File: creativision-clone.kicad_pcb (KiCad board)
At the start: 2 copper layers, 205.7 x 99.7 mm, 103 parts, among them J1 Conn_01x10_Socket, J2 Conn_01x10_Socket, J3 Conn_01x07_Pin, J4 Conn_01x04_Socket, J5 RCJ-013, J6 RCJ-014, P1 Cartridge Slot, Q1 2n4401, SW1 Reset, SW2 Power Toggle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

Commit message: Data bus and control signals laid out on cart
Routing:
- net -5V: track 0.00 -> 136.7 mm, vias 0 -> 2
- net /~{WRAM_CE}: track 35.1 -> 164.5 mm, vias 1 -> 6
- net /~{ROM1}: track 0.00 -> 118.3 mm, vias 0 -> 5
- net /~{ROM_RD}: track 13.4 -> 130.0 mm, vias 2 -> 7
- net /~{ROM0}: track 0.00 -> 105.6 mm, vias 0 -> 2
- net /~{ROM2}: track 0.00 -> 105.2 mm, vias 0 -> 4
- net /R/~{W}: track 136.2 -> 232.8 mm, vias 7 -> 9
- net /AUDIO_IN: track 139.3 -> 233.7 mm, vias 1 -> 3
- net +12V: track 0.00 -> 73.2 mm, vias 0 -> 1
- net /d6: track 176.5 -> 248.5 mm, vias 10 -> 12
- net /Φ2: track 122.6 -> 193.9 mm, vias 4 -> 6
- net /d7: track 198.3 -> 269.0 mm, vias 10 -> 12
- net /d4: track 147.1 -> 207.7 mm, vias 10 -> 12
- net /d5: track 156.6 -> 215.7 mm, vias 8 -> 10
- net /d3: track 153.3 -> 205.7 mm, vias 6 -> 8
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
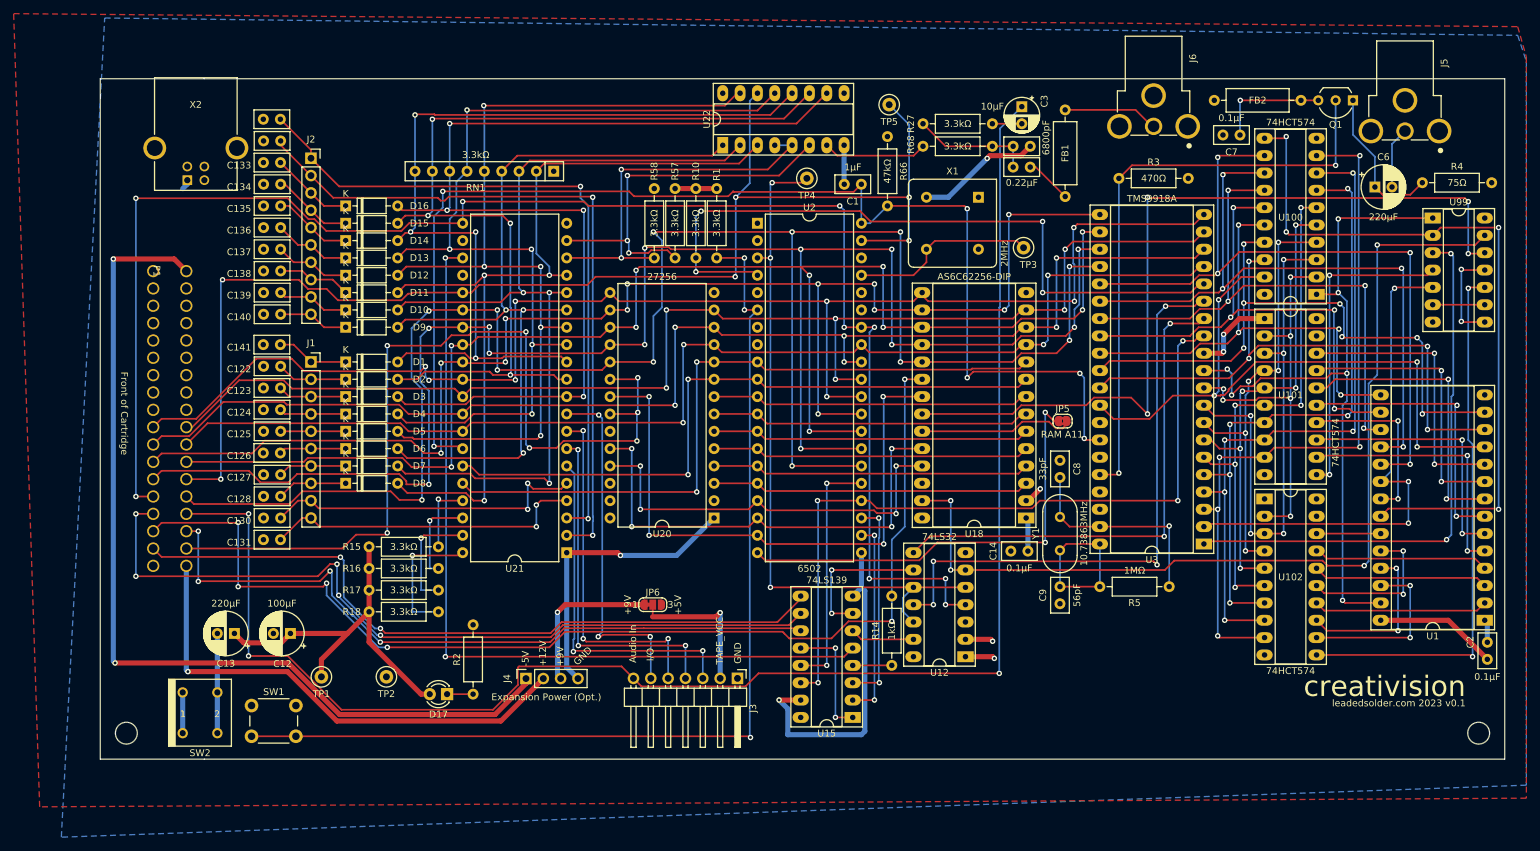
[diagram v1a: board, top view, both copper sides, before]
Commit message: Power pour problems
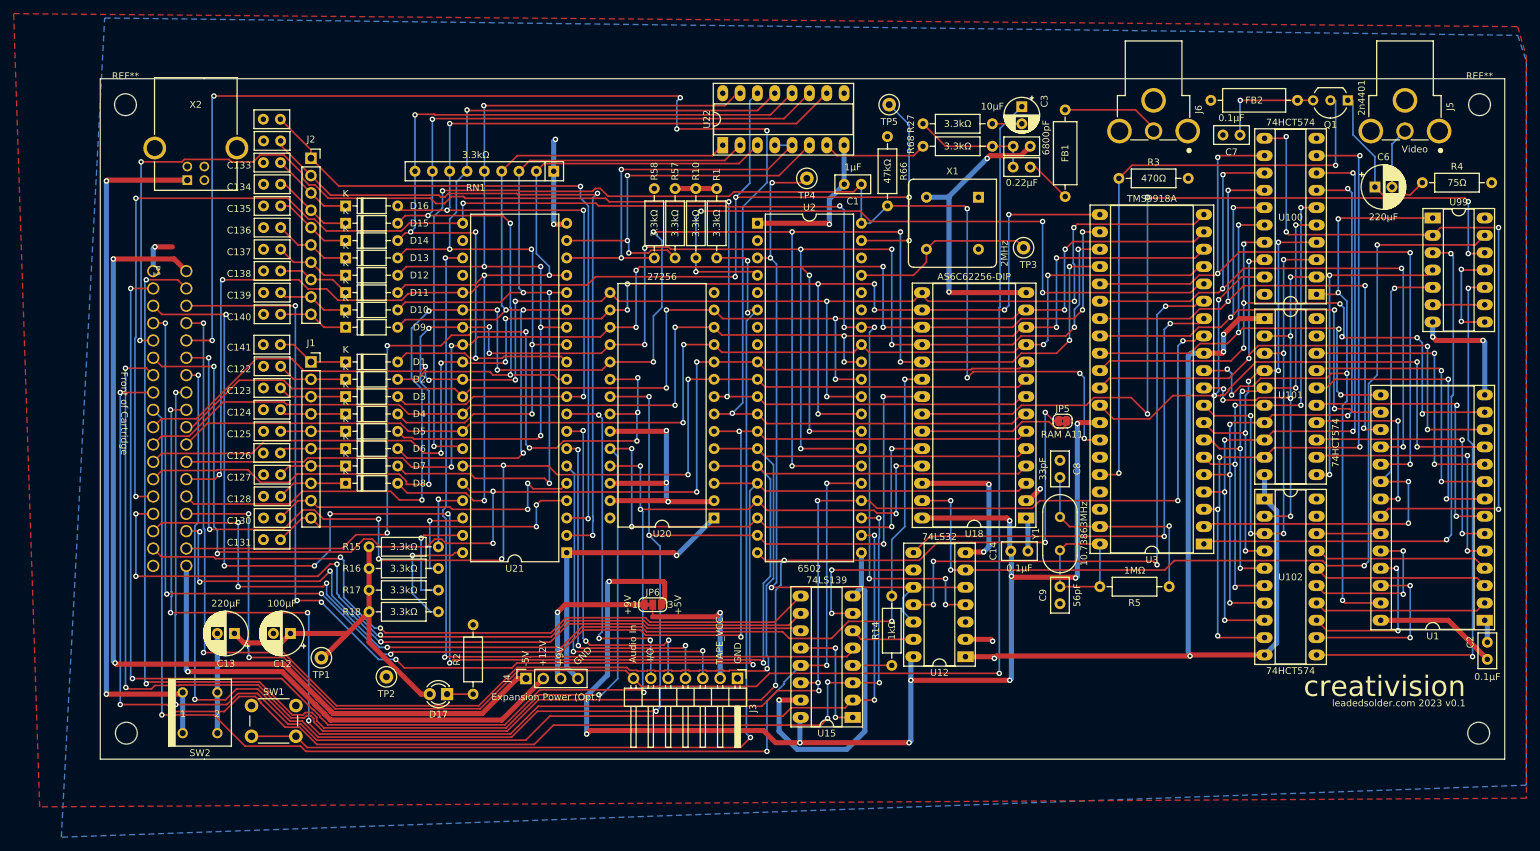
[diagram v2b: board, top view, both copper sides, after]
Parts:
- added REF**: MountingHole_3.2mm_M3, MountingHole:MountingHole_3.2mm_M3, F.Cu at (267.7, 47.4)
- added REF**: MountingHole_3.2mm_M3, MountingHole:MountingHole_3.2mm_M3, F.Cu at (69.3, 47.4)
- moved TP1 2.79 mm to (98.0, 128.4)
- moved Q1 0.76 mm to (248.4, 46.8)
- moved J6 0.69 mm to (220.0, 45.3)
- moved FB2 0.51 mm to (228.3, 46.8)
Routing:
- net GND: track 147.7 -> 389.8 mm, vias 8 -> 18
- net +5V: track 80.5 -> 285.4 mm, vias 0 -> 13
- net /a6: track 46.7 -> 232.2 mm, vias 0 -> 7
- net /a9: track 69.8 -> 245.2 mm, vias 4 -> 7
- net /a5: track 46.7 -> 220.3 mm, vias 0 -> 3
- net /a11: track 65.2 -> 237.0 mm, vias 2 -> 6
- net /a3: track 46.9 -> 216.7 mm, vias 0 -> 6
- net /a13: track 30.7 -> 199.8 mm, vias 2 -> 6
- net /a8: track 60.4 -> 228.0 mm, vias 4 -> 7
- net /a4: track 46.7 -> 208.2 mm, vias 0 -> 6
- net /a7: track 46.7 -> 204.4 mm, vias 0 -> 5
- net /a12: track 29.2 -> 181.7 mm, vias 2 -> 4
- net /a15: track 35.6 -> 186.3 mm, vias 2 -> 4
- net /a10: track 88.3 -> 237.2 mm, vias 4 -> 7
- net /a14: track 110.1 -> 257.9 mm, vias 4 -> 9
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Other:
- board text added: "Video"

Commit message: More plane problems
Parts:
- moved REF** 1.80 mm to (67.6, 47.1)
- moved REF** 1.65 mm to (67.8, 139.5)
- moved REF** 1.52 mm to (269.2, 47.4)
- moved REF** 1.40 mm to (269.0, 139.5)
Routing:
- net GND: track 389.8 -> 415.8 mm
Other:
- board size 205.7 x 99.7 mm -> 208.8 x 99.7 mm
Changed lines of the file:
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@@
         (effects (font (size 1 1) (thickness 0.15)))
     )
-    (fp_text value "AS6C62256-DIP" (at 7.62 35.35) (layer "F.Fab")
+    (fp_text value "AS6C62256-DIP" (at 7.62 35.35) (layer "F.SilkS")
         (effects (font (size 1 1) (thickness 0.15)))
     )
@@
   )
   (footprint "MountingHole:MountingHole_3.2mm_M3" locked (layer "F.Cu")
-    (at 267.59 139.472929)
+    (at 268.987 139.472929)
     (descr "Mounting Hole 3.2mm, no annular, M3")
     (tags "mounting hole 3.2mm no annular m3")
@@
   )
   (footprint "MountingHole:MountingHole_3.2mm_M3" (layer "F.Cu")
-    (at 267.717 47.397929)
+    (at 269.241 47.397929)
     (descr "Mounting Hole 3.2mm, no annular, M3")
     (tags "mounting hole 3.2mm no annular m3")
@@
   )
   (footprint "MountingHole:MountingHole_3.2mm_M3" locked (layer "F.Cu")
-    (at 69.47 139.472929)
+    (at 67.819 139.472929)
     (descr "Mounting Hole 3.2mm, no annular, M3")
     (tags "mounting hole 3.2mm no annular m3")
@@
   )
   (footprint "MountingHole:MountingHole_3.2mm_M3" (layer "F.Cu")
-    (at 69.343 47.397929)
+    (at 67.565 47.143929)
     (descr "Mounting Hole 3.2mm, no annular, M3")
     (tags "mounting hole 3.2mm no annular m3")
@@
     )
   )
-  (gr_line (start 271.4 143.282929) (end 271.4 43.587929)
+  (gr_line (start 65.66 143.282929) (end 64.009 143.282929)
+    (stroke (width 0.1) (type default)) (layer "Edge.Cuts"))
+  (gr_line (start 272.797 143.282929) (end 272.797 43.587929)
+    (stroke (width 0.1) (type default)) (layer "Edge.Cuts"))
+  (gr_line (start 64.009 43.587929) (end 64.009 143.282929)
+    (stroke (width 0.1) (type default)) (layer "Edge.Cuts"))
+  (gr_line (start 272.797 43.587929) (end 271.4 43.587929)
+    (stroke (width 0.1) (type default)) (layer "Edge.Cuts"))
+  (gr_line (start 65.66 43.587929) (end 64.009 43.587929)
     (stroke (width 0.1) (type default)) (layer "Edge.Cuts"))
-  (gr_line (start 65.66 43.587929) (end 65.66 143.282929)
+  (gr_line (start 272.797 143.282929) (end 271.4 143.282929)
     (stroke (width 0.1) (type default)) (layer "Edge.Cuts"))
   (gr_line (start 80.9 43.587929) (end 65.66 43.587929)
@@
   (segment (start 195.835 112.167929) (end 195.073 112.929929) (width 0.75) (layer "B.Cu") (net 2))
   (segment (start 174.625 59.035) (end 174.645 59.055) (width 0.75) (layer "B.Cu") (net 2))
+  (segment (start 225.045 84.227929) (end 225.045 58.192929) (width 0.75) (layer "B.Cu") (net 2))
   (segment (start 195.835 103.023929) (end 195.835 112.167929) (width 0.75) (layer "B.Cu") (net 2))
   (segment (start 172.467 64.923929) (end 172.467 61.233) (width 0.75) (layer "B.Cu") (net 2))
@@
   (segment (start 125.731 139.599929) (end 97.791706 139.599929) (width 0.25) (layer "F.Cu") (net 110))
   (segment (start 177.165 105.41) (end 170.7255 105.41) (width 0.25) (layer "F.Cu") (net 110))
-  (segment (start 226.685 81.275) (end 225.9605 81.9995) (width 0.25) (layer "F.Cu") (net 110))
   (segment (start 96.192905 137.896024) (end 96.192905 137.642023) (width 0.25) (layer "F.Cu") (net 110))
   (segment (start 178.29637 105.41) (end 177.165 105.41) (width 0.25) (layer "F.Cu") (net 110))
   (segment (start 129.795 135.535929) (end 125.731 139.599929) (width 0.25) (layer "F.Cu") (net 110))
   (segment (start 96.013 121.819929) (end 75.947 121.819929) (width 0.25) (layer "F.Cu") (net 110))
-  (segment (start 225.9605 81.9995) (end 224.26226 81.9995) (width 0.25) (layer "F.Cu") (net 110))
+  (segment (start 226.685 81.275) (end 225.9605 81.9995) (width 0.25) (layer "F.Cu") (net 110))
+  (segment (start 225.9605 81.9995) (end 224.0705 81.9995) (width 0.25) (layer "F.Cu") (net 110))
   (segment (start 223.52 105.41) (end 203.28599 105.41) (width 0.25) (layer "F.Cu") (net 110))
   (segment (start 164.847 133.249929) (end 162.561 135.535929) (width 0.25) (layer "F.Cu") (net 110))
@@
   (segment (start 203.28599 105.41) (end 202.16099 106.535) (width 0.25) (layer "F.Cu") (net 110))
   (segment (start 162.561 135.535929) (end 129.795 135.535929) (width 0.25) (layer "F.Cu") (net 110))
-  (segment (start 227.335 81.275) (end 226.685 81.275) (width 0.25) (layer "F.Cu") (net 110))
   (segment (start 202.16099 106.535) (end 179.42137 106.535) (width 0.25) (layer "F.Cu") (net 110))
   (segment (start 97.791706 139.599929) (end 96.140353 137.948576) (width 0.25) (layer "F.Cu") (net 110))
   (segment (start 170.943 133.249929) (end 164.847 133.249929) (width 0.25) (layer "F.Cu") (net 110))
+  (segment (start 227.335 81.275) (end 226.685 81.275) (width 0.25) (layer "F.Cu") (net 110))
   (segment (start 96.140353 137.948576) (end 96.192905 137.896024) (width 0.25) (layer "F.Cu") (net 110))
   (via (at 170.7255 105.41) (size 0.8) (drill 0.4) (layers "F.Cu" "B.Cu") (net 110))
   (via (at 96.192905 137.642023) (size 0.8) (drill 0.4) (layers "F.Cu" "B.Cu") (net 110))
   (via (at 223.52 105.41) (size 0.8) (drill 0.4) (layers "F.Cu" "B.Cu") (net 110))
-  (via (at 224.26226 81.9995) (size 0.8) (drill 0.4) (layers "F.Cu" "B.Cu") (net 110))
+  (via (at 224.0705 81.9995) (size 0.8) (drill 0.4) (layers "F.Cu" "B.Cu") (net 110))
   (via (at 96.013 121.819929) (size 0.8) (drill 0.4) (layers "F.Cu" "B.Cu") (net 110))
   (via (at 170.815 132.08) (size 0.8) (drill 0.4) (layers "F.Cu" "B.Cu") (net 110))
@@
   (via (at 170.943 133.249929) (size 0.8) (drill 0.4) (layers "F.Cu" "B.Cu") (net 110))
   (via (at 75.947 92.101929) (size 0.8) (drill 0.4) (layers "F.Cu" "B.Cu") (net 110))
-  (segment (start 223.52 82.74176) (end 224.26226 81.9995) (width 0.25) (layer "B.Cu") (net 110))
   (segment (start 76.049513 119.467829) (end 76.121309 119.396033) (width 0.25) (layer "B.Cu") (net 110))
   (segment (start 170.815 105.4995) (end 170.7255 105.41) (width 0.25) (layer "B.Cu") (net 110))
   (segment (start 170.815 132.08) (end 170.815 105.4995) (width 0.25) (layer "B.Cu") (net 110))
+  (segment (start 223.52 105.41) (end 223.52 82.55) (width 0.25) (layer "B.Cu") (net 110))
   (segment (start 76.121309 119.396033) (end 76.121309 118.795837) (width 0.25) (layer "B.Cu") (net 110))
   (segment (start 170.815 132.08) (end 170.815 133.121929) (width 0.25) (layer "B.Cu") (net 110))
   (segment (start 96.192905 137.642023) (end 96.192905 121.999834) (width 0.25) (layer "B.Cu") (net 110))
+  (segment (start 223.52 82.55) (end 224.0705 81.9995) (width 0.25) (layer "B.Cu") (net 110))
   (segment (start 75.947 121.819929) (end 76.049513 121.717416) (width 0.25) (layer "B.Cu") (net 110))
   (segment (start 76.049513 118.724041) (end 76.049513 92.204442) (width 0.25) (layer "B.Cu") (net 110))
@@
   (segment (start 76.049513 92.204442) (end 75.947 92.101929) (width 0.25) (layer "B.Cu") (net 110))
   (segment (start 76.049513 121.717416) (end 76.049513 119.467829) (width 0.25) (layer "B.Cu") (net 110))
-  (segment (start 223.52 105.41) (end 223.52 82.74176) (width 0.25) (layer "B.Cu") (net 110))
   (segment (start 96.192905 121.999834) (end 96.013 121.819929) (width 0.25) (layer "B.Cu") (net 110))
   (segment (start 76.121309 118.795837) (end 76.049513 118.724041) (width 0.25) (layer "B.Cu") (net 110))
@@
   )
   (zone (net 2) (net_name "GND") (layer "B.Cu") (hatch edge 0.5)
-    (connect_pads (clearance 0.5))
+    (connect_pads yes (clearance 0.5))
     (min_thickness 0.25) (filled_areas_thickness no)
     (fill yes (thermal_gap 0.5) (thermal_bridge_width 0.5))

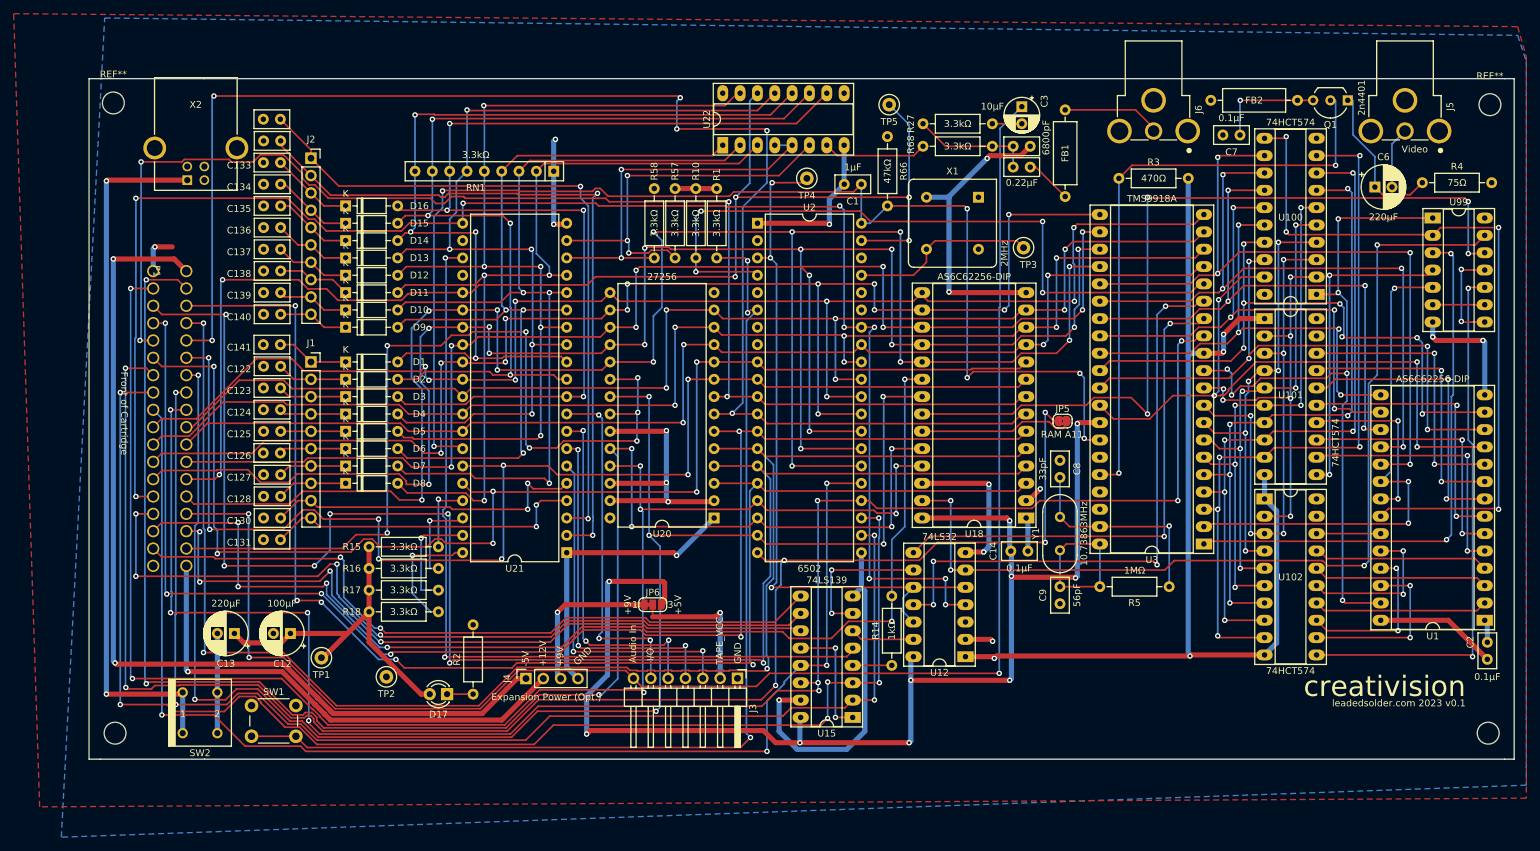
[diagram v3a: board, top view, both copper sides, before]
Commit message: Placed and routed, 0 DRC
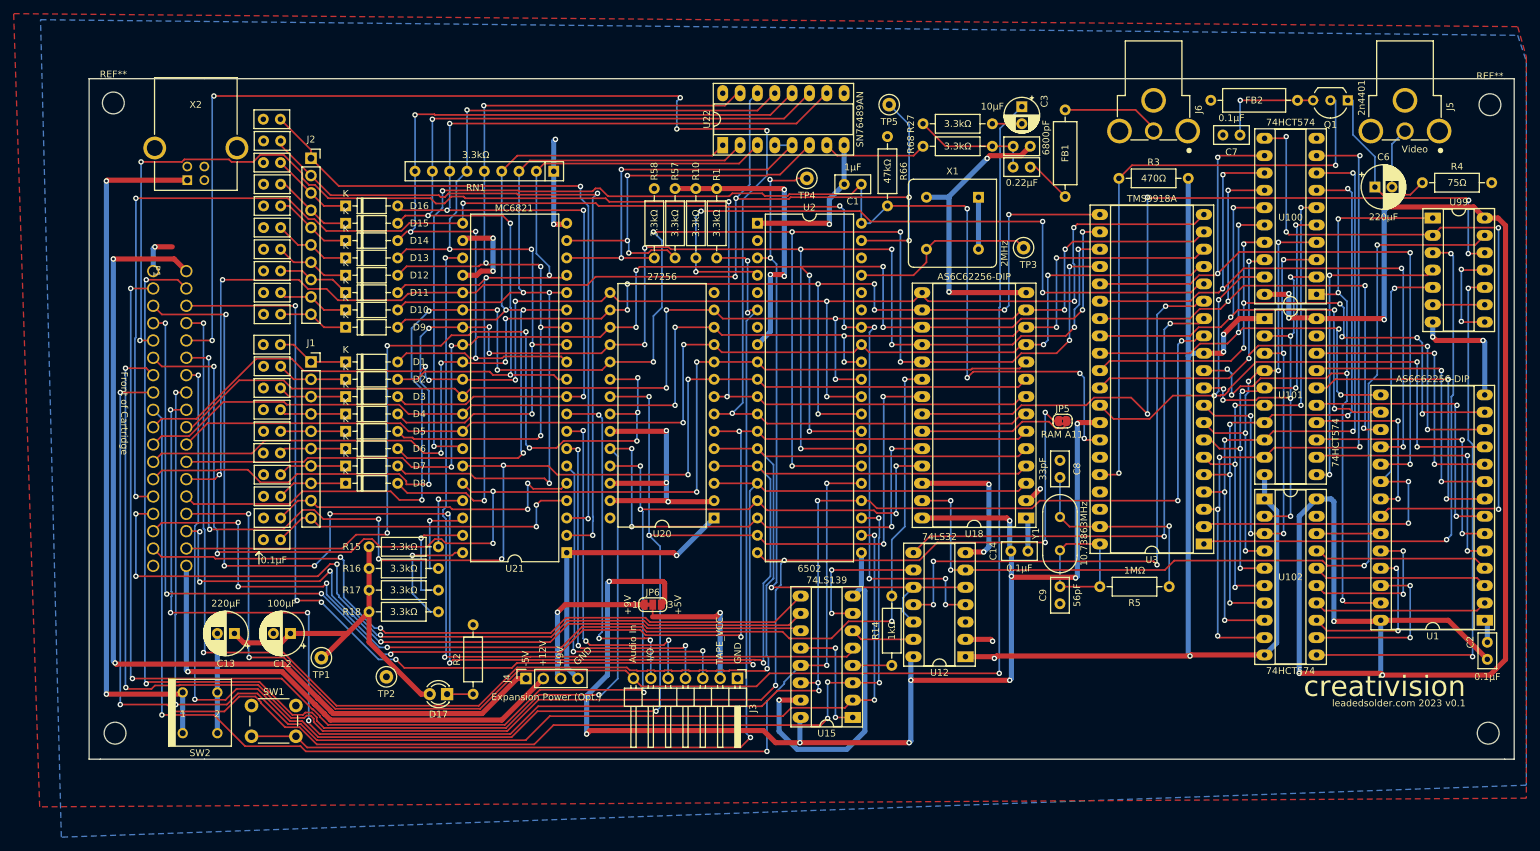
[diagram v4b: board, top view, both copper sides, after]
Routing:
- net +5V: track 285.4 -> 556.1 mm, vias 13 -> 25
- net /Φ1: track 102.2 -> 102.8 mm
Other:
- board text added: "0.1µF"
- board text added: "MC6821"
